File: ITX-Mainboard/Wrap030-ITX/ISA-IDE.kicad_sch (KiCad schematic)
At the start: 21 parts, among them U13 74LS573, U14 74LS573, U15 74LS573, U16 74AHCT244, U17 ATF1504, U18 74HCT688, U19 74LS139, U5 74HC245

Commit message: PCB substantial completion
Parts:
- removed U16: 74AHCT244, Package_DIP:DIP-20_W7.62mm_Socket, symbol 74xx:74AHCT244
- removed unit 1 of U19
- added U16: 74HC245, Package_DIP:DIP-20_W7.62mm_Socket, symbol 74xx:74HC245
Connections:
- net CPU-A16: now also U15.6 (D4); no longer U15.2 (D0)
- net CPU-A17: now also U15.7 (D5), U16.2 (A0); no longer U15.3 (D1)
- net CPU-A18: now also U15.8 (D6), U16.3 (A1); no longer U15.4 (D2)
- net CPU-A19: now also U15.9 (D7), U16.4 (A2); no longer U15.5 (D3)
- net CPU-A20: now also U16.5 (A3)
- net CPU-A21: now also U16.6 (A4)
- net CPU-A22: now also U16.7 (A5)
- net CPU-A23: now also U16.8 (A6)
- net CPU-D24: now also U5.11 (B7); no longer U5.18 (B0)
- net CPU-D25: now also U5.12 (B6); no longer U5.17 (B1)
- net CPU-D26: now also U5.13 (B5); no longer U5.16 (B2)
- net CPU-D27: now also U5.14 (B4); no longer U5.15 (B3)
- net CPU-D28: now also U5.15 (B3); no longer U5.14 (B4)
- net CPU-D29: now also U5.16 (B2); no longer U5.13 (B5)
- net CPU-D30: now also U5.17 (B1); no longer U5.12 (B6)
- net CPU-D31: now also U5.18 (B0); no longer U5.11 (B7)
- net GND: now also U15.2 (D0), U15.3 (D1), U15.4 (D2), U15.5 (D3), U16.10 (GND), U16.9 (A7); no longer U15.6 (D4), U15.7 (D5), U15.8 (D6), U15.9 (D7)
- net ISA-A16: now also U15.15 (Q4); no longer U15.19 (Q0)
- net ISA-A17: now also U15.14 (Q5); no longer U15.18 (Q1)
- net ISA-A18: now also U15.13 (Q6); no longer U15.17 (Q2)
- net ISA-A19: now also U15.12 (Q7); no longer U15.16 (Q3)
- net ISA-A7: now also U18.13 (P5); no longer U18.11 (P4)
- net ISA-A8: now also U18.11 (P4); no longer U18.13 (P5)
- net ISA-A9: now also U17.39 (IO57)
- net ISA-AEN: now also U16.19 (CE)
- net ISA-ALE: now also U17.28 (IO40); no longer U17.21 (IO17)
- net ISA-CLK: now also U17.14 (IO30); no longer U17.25 (IO35)
- net ISA-D10: now also U5.7 (A5); no longer U5.4 (A2)
- net ISA-D11: now also U5.6 (A4); no longer U5.5 (A3)
- net ISA-D12: now also U5.5 (A3); no longer U5.6 (A4)
- net ISA-D13: now also U5.4 (A2); no longer U5.7 (A5)
- net ISA-D14: now also U5.3 (A1); no longer U5.8 (A6)
- net ISA-D15: now also U5.2 (A0); no longer U5.9 (A7)
- net ISA-D8: now also U5.9 (A7); no longer U5.2 (A0)
- net ISA-D9: now also U5.8 (A6); no longer U5.3 (A1)
- net ISA-IORDY: now also U17.27 (IO37); no longer U17.29 (IO41)
- net ISA-LA17: now also U16.18 (B0)
- net ISA-LA18: now also U16.17 (B1)
- net ISA-LA19: now also U16.16 (B2)
- net ISA-LA20: now also U16.15 (B3)
- net ISA-LA21: now also U16.14 (B4)
- net ISA-LA22: now also U16.13 (B5)
- net ISA-LA23: now also U16.12 (B6)
- net ISA-MASTER: now also U17.18 (IO21); no longer U17.28 (IO40)
- net ISA-SBHE: now also U17.16 (IO25); no longer U17.18 (IO21)
- net R/~{W}: now also U17.33 (IO49); no longer U17.6 (IO11)
- net SIZ0: now also U17.8 (IO5); no longer U17.12 (IO1)
- net SIZ1: now also U17.6 (IO11); no longer U17.11 (IO3)
- net VCC: now also U16.1 (A->B), U16.20 (VCC)
- net ~{AS}: now also U17.34 (IO51); no longer U17.9 (IO4)
- net ~{DS}: now also U17.31 (IO46); no longer U17.8 (IO5)
- net ~{IDE-CS1}: now also U17.40 (IO62)
- net ~{IDE-CS3}: now also U17.41 (IO64)
- net ~{ISA-CE}: now also U17.9 (IO4); no longer U17.31 (IO46)
- net ~{ISA-DACK16}: now also U17.12 (IO1); no longer U17.34 (IO51)
- net ~{ISA-DACK8}: now also U17.11 (IO3); no longer U17.33 (IO49)
- net ~{ISA-IOCS16}: now also U17.36 (IO52); no longer U17.27 (IO37)
- net ~{ISA-IOR}: now also U17.21 (IO17); no longer U17.24 (IO33)
- net ~{ISA-IOW}: now also U17.24 (IO33); no longer U17.14 (IO30)
- net ~{ISA-MEMCS16}: now also U17.37 (IO53); no longer U17.26 (IO36)
- net ~{ISA-MEMR}: now also U17.25 (IO35); no longer U17.17 (IO24)
- net ~{ISA-MEMW}: now also U17.26 (IO36); no longer U17.16 (IO25)
- net ~{IDE-CS}: now reaches U18.19 (P=R)
- net ~{IDE-CS}: now also U17.17 (IO24)
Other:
- moved on the sheet: C1, C15

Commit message: Add interrupt controller to schematic
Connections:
- net ISA-MASTER: now also U17.19 (IO20); no longer U17.18 (IO21)
- net ISA-RESET: now also U17.17 (IO24); no longer U17.19 (IO20)
- net ISA-SBHE: now also U17.18 (IO21); no longer U17.16 (IO25)
- net ~{IDE-CS}: now also U17.16 (IO25); no longer U17.17 (IO24)
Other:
- moved on the sheet: C1, C15

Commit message: Completing PCB Routing
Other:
- title: Wrap030 ITX -> Wrap030-ATX Mainboard
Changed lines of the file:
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@@
   (paper "USLetter")
   (title_block
-    (title "Wrap030 ITX")
-    (date "2023-03-15")
-    (rev "0")
+    (title "Wrap030-ATX Mainboard")
+    (date "2023-03-26")
+    (rev "1")
     (company "techav")
   )

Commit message: PCB Silkscreen & DRC Cleanup
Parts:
- added C31: 100nF, Capacitor_SMD:C_0402_1005Metric_Pad0.74x0.62mm_HandSolder, symbol Device:C_Small
- added X2: 14.3181M, Oscillator:Oscillator_DIP-8, symbol Oscillator:CXO_DIP8
- U13, U14, U15: value 74LS573 -> 74ACT573
- U16, U5: value 74HC245 -> 74ACT245
- U17: value ATF1504 -> ATF1504AS
- U18: value 74HCT688 -> 74ACT688
- U19: value 74LS139 -> 74ACT139
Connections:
- net GND: now also C31.2, X2.4 (GND)
- net VCC: now also C31.1, X2.8 (Vcc)
- new net ISA-OSC: X2.5 (OUT)

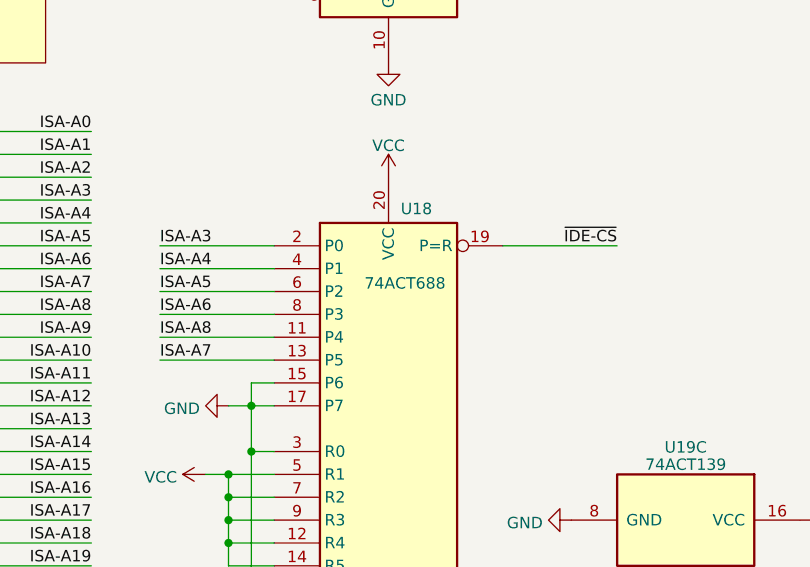
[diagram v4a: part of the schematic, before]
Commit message: Replace resistor nets with 0402 & update gerbers
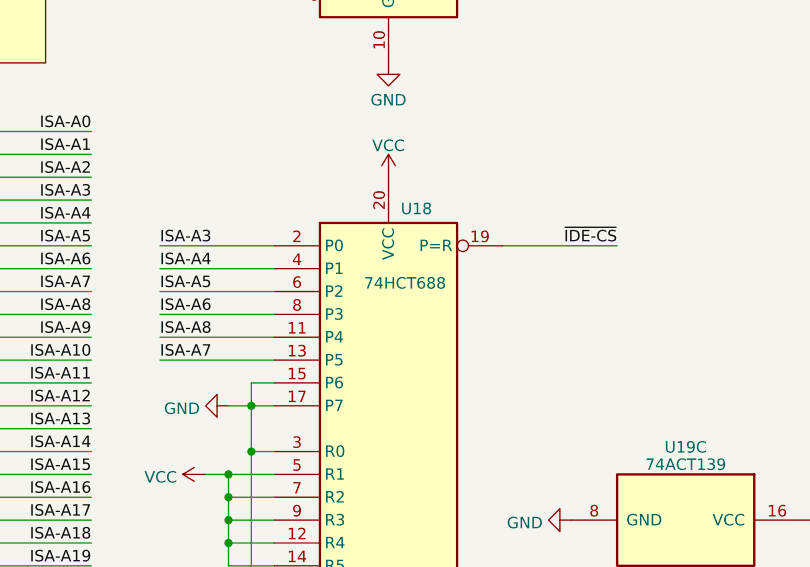
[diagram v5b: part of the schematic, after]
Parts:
- C1, C31: Mouser-Part (none) -> 187-CL05B104KO5NNNC; Notes (none) -> JLC
- C15: Mouser-Part (none) -> 187-CL05A105KA5NQNC; Notes (none) -> JLC
- U13, U14, U15: Mouser-Part (none) -> 595-SN74ACT573N; Notes (none) -> OFE; Socket-Mouser (none) -> 571-1-2199298-6
- U16, U5: Mouser-Part (none) -> 595-SN74ACT245N; Notes (none) -> OFE; Socket-Mouser (none) -> 571-1-2199298-6
- U17: Mouser-Part (none) -> 556-AF1500A10JU; Notes (none) -> OFE; Socket-Mouser (none) -> 151-1545
- U18: value 74ACT688 -> 74HCT688; Mouser-Part (none) -> 595-CD74HCT688EE4; Notes (none) -> OFE; Socket-Mouser (none) -> 571-1-2199298-6
- U19: Mouser-Part (none) -> 595-CD74ACT139E; Notes (none) -> OFE; Socket-Mouser (none) -> 571-1-2199298-4
- X2: Notes (none) -> Mouser
